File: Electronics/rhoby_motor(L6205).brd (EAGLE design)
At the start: 80 x 79.7 mm, 71 parts, among them IC1 L6205PD, IC2 L6205PD, IC3 L6205PD, IC4 74AC14D, IC5 L6205PD, IC6 74AC14D, J1 22-27-2041-04, J23 22-27-2041-04, J3 22-27-2041-04, J5 22-27-2041-04, J7 22-27-2041-04

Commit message: Changed some connectors
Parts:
- removed SV1, SV3: (no value), con-lstb:MA08-2
- removed SV2: (no value), con-lstb:MA08-1
- removed SV4: (no value), con-lstb:MA04-2
- removed SV5, SV6, SV7, SV8: (no value), con-lstb:MA06-1
- added JP11, JP12, JP13, JP14: (no value), pinhead:1X06
- added JP15: (no value), pinhead:2X08
- added JP16: (no value), pinhead:2X04
- added JP17, JP18, JP19, JP20: (no value), pinhead:2X03
- moved C2 158.0 mm to (49.5, 28.6), flipped to the bottom, turned to 90 degrees
- moved C1 157.0 mm to (59.7, 46.4), flipped to the bottom, turned to 90 degrees
- moved C9 156.9 mm to (69.2, 29.8), flipped to the bottom, turned to 90 degrees
- moved C26 151.0 mm to (59.1, 52.7), flipped to the bottom
- moved JP8 150.7 mm to (71.1, 50.8), turned to 270 degrees
- moved C25 150.4 mm to (63.5, 57.1), flipped to the bottom
- moved C21 145.1 mm to (57.8, 72.4), flipped to the bottom
- moved JP7 143.5 mm to (71.1, 55.9), turned to 270 degrees
- moved C8 131.6 mm to (73.0, 2.54), flipped to the bottom
- moved C13 129.3 mm to (64.8, 2.54), flipped to the bottom
- moved JP4 126.5 mm to (52.1, 8.89), turned to 180 degrees
- moved JP3 125.5 mm to (57.1, 8.89), turned to 180 degrees
- moved C3 123.3 mm to (30.5, 19.1), flipped to the bottom
- moved C15 120.8 mm to (36.2, 61.0), flipped to the bottom, turned to 180 degrees
- moved C14 119.8 mm to (45.7, 2.54), flipped to the bottom
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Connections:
- net +5V: now also JP17.3, JP17.4, JP18.3, JP18.4, JP19.3, JP19.4, JP20.3, JP20.4; no longer SV1.1, SV1.11, SV1.13, SV1.15, SV1.3, SV1.5, SV1.7, SV1.9
- net ENC1_IN: now also JP15.1; no longer SV3.1
- net ENC2_IN: now also JP15.9; no longer SV3.9
- net ENC3_IN: now also JP15.2; no longer SV3.2
- net ENC4_IN: now also JP15.10; no longer SV3.10
- net GND: now also JP15.11, JP15.12, JP15.15, JP15.16, JP15.3, JP15.4, JP15.7, JP15.8, JP17.5, JP17.6, JP18.5, JP18.6, JP19.5, JP19.6, JP20.5, JP20.6; no longer SV1.10, SV1.12, SV1.14, SV1.16, SV1.2, SV1.4, SV1.6, SV1.8, SV3.11, SV3.12, SV3.15, SV3.16, SV3.3, SV3.4, SV3.7, SV3.8
- net HALL1: now also JP16.1; no longer SV4.1
- net HALL1_IN: now also JP17.1; no longer SV2.1
- net HALL2: now also JP16.3; no longer SV4.3
- net HALL2_IN: now also JP17.2; no longer SV2.2
- net HALL3: now also JP16.5; no longer SV4.5
- net HALL3_IN: now also JP18.1; no longer SV2.3
- net HALL4: now also JP16.7; no longer SV4.7
- net HALL4_IN: now also JP18.2; no longer SV2.4
- net HALL5: now also JP16.2; no longer SV4.2
- net HALL5_IN: now also JP19.1; no longer SV2.5
- net HALL6: now also JP16.4; no longer SV4.4
- net HALL6_IN: now also JP19.2; no longer SV2.6
- net HALL7: now also JP16.6; no longer SV4.6
- net HALL7_IN: now also JP20.1; no longer SV2.7
- net HALL8: now also JP16.8; no longer SV4.8
- net HALL8_IN: now also JP20.2; no longer SV2.8
- net N$1: now also JP13.1; no longer SV5.1
- net N$15: now also JP13.6; no longer SV5.6
- net N$16: now also JP13.3; no longer SV5.3
- net N$2: now also JP13.2; no longer SV5.2
- net N$29: now also JP11.1; no longer SV7.1
- net N$30: now also JP11.2; no longer SV7.2
- net N$32: now also JP11.4; no longer SV7.4
- net N$33: now also JP11.5; no longer SV7.5
- net N$34: now also JP11.6; no longer SV7.6
- net N$35: now also JP11.3; no longer SV7.3
- net N$4: now also JP13.4; no longer SV5.4
- net N$42: now also JP14.1; no longer SV6.1
- net N$43: now also JP14.2; no longer SV6.2
- net N$45: now also JP14.4; no longer SV6.4
- net N$46: now also JP14.5; no longer SV6.5
- net N$47: now also JP14.6; no longer SV6.6
- net N$48: now also JP14.3; no longer SV6.3
- net N$58: now also JP12.1; no longer SV8.1
- net N$59: now also JP12.2; no longer SV8.2
- net N$61: now also JP12.4; no longer SV8.4
- net N$62: now also JP12.5; no longer SV8.5
- net N$63: now also JP12.6; no longer SV8.6
- net N$64: now also JP12.3; no longer SV8.3
- net N$7: now also JP13.5; no longer SV5.5
- net N$77: now also JP15.13; no longer SV3.13
- net N$78: now also JP15.5; no longer SV3.5
- net N$79: now also JP15.6; no longer SV3.6
- net N$80: now also JP15.14; no longer SV3.14

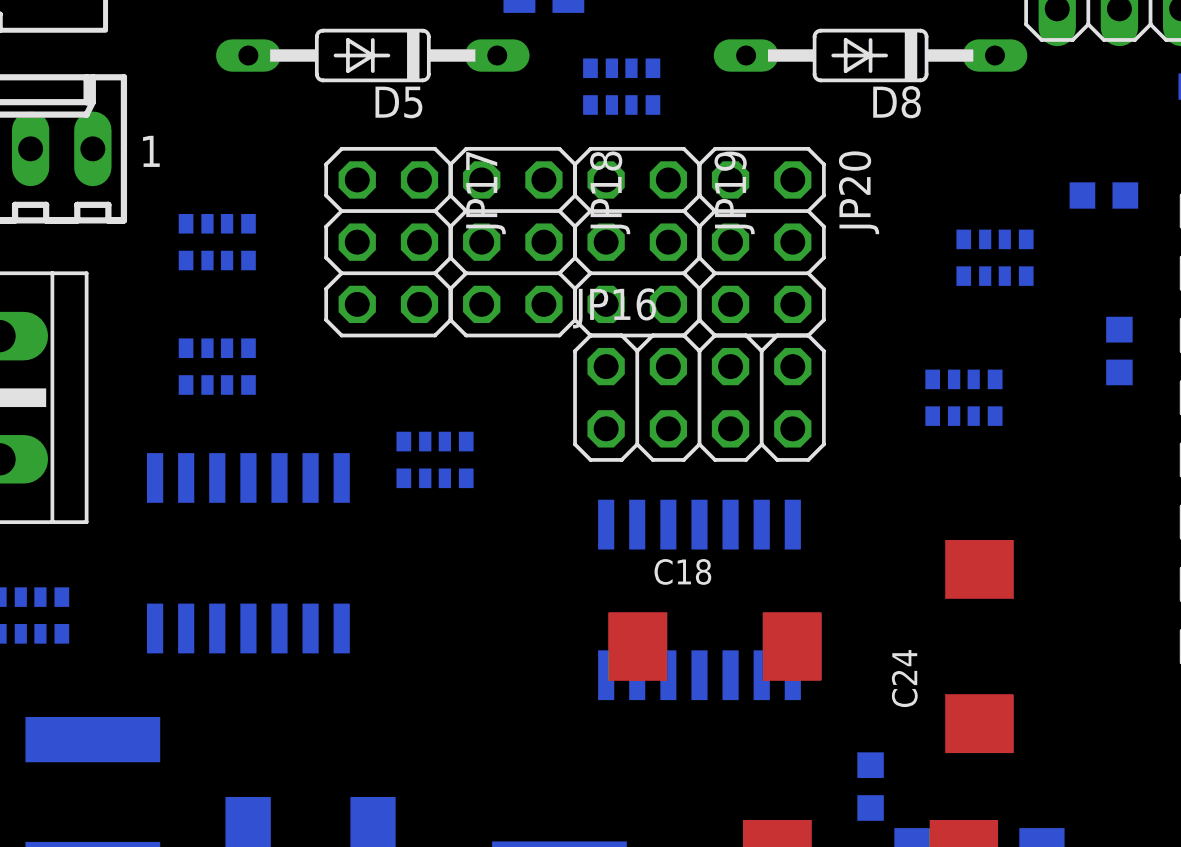
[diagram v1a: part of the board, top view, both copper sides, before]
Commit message: Moved some components on bottom
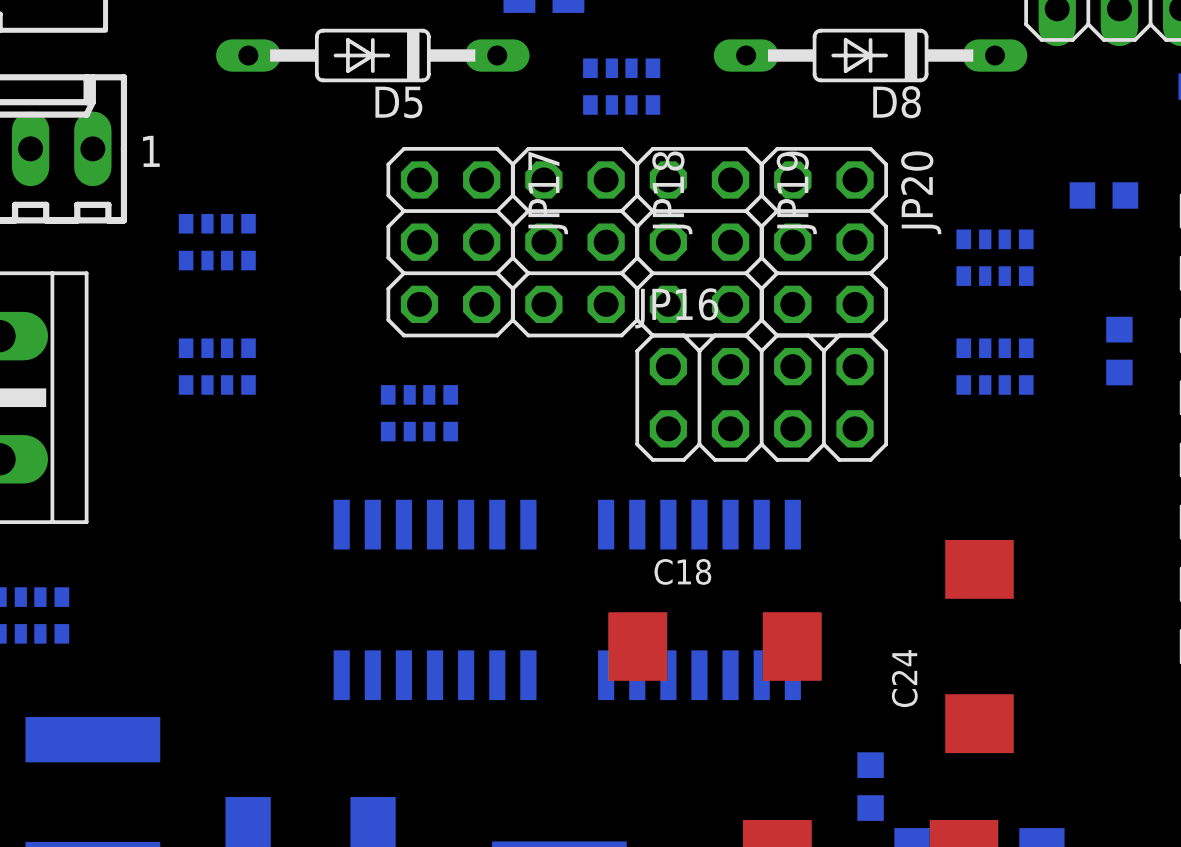
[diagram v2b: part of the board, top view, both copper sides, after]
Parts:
- moved IC4 7.85 mm to (31.8, 36.2), turned to 180 degrees
- moved JP18 2.54 mm to (37.5, 50.8)
- moved JP16 2.54 mm to (45.1, 44.5)
- moved JP17 2.54 mm to (32.4, 50.8)
- moved JP19 2.54 mm to (42.5, 50.8)
- moved JP20 2.54 mm to (47.6, 50.8)
- moved RN10 2.01 mm to (31.1, 43.8)
- moved RN5 1.80 mm to (54.6, 45.7)
